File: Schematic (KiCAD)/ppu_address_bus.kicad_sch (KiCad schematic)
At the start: 59 parts, among them X3 INVERT

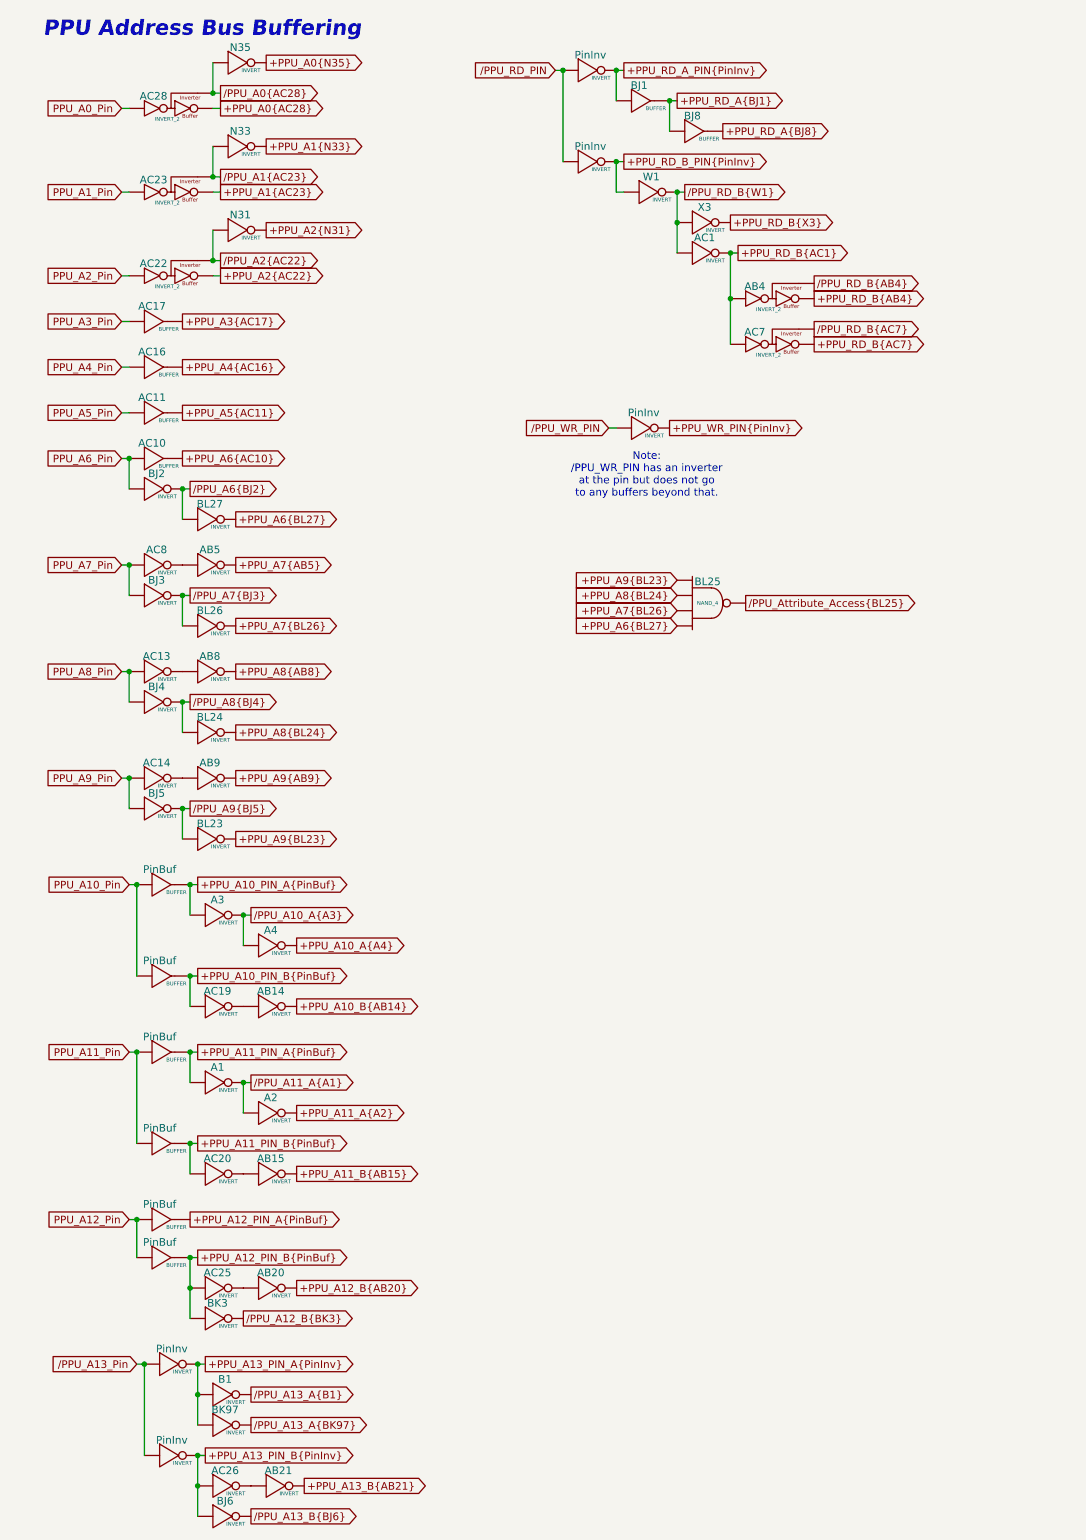
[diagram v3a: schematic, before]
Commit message: - All known gates and traces are now accounted for in the schematics!  :)
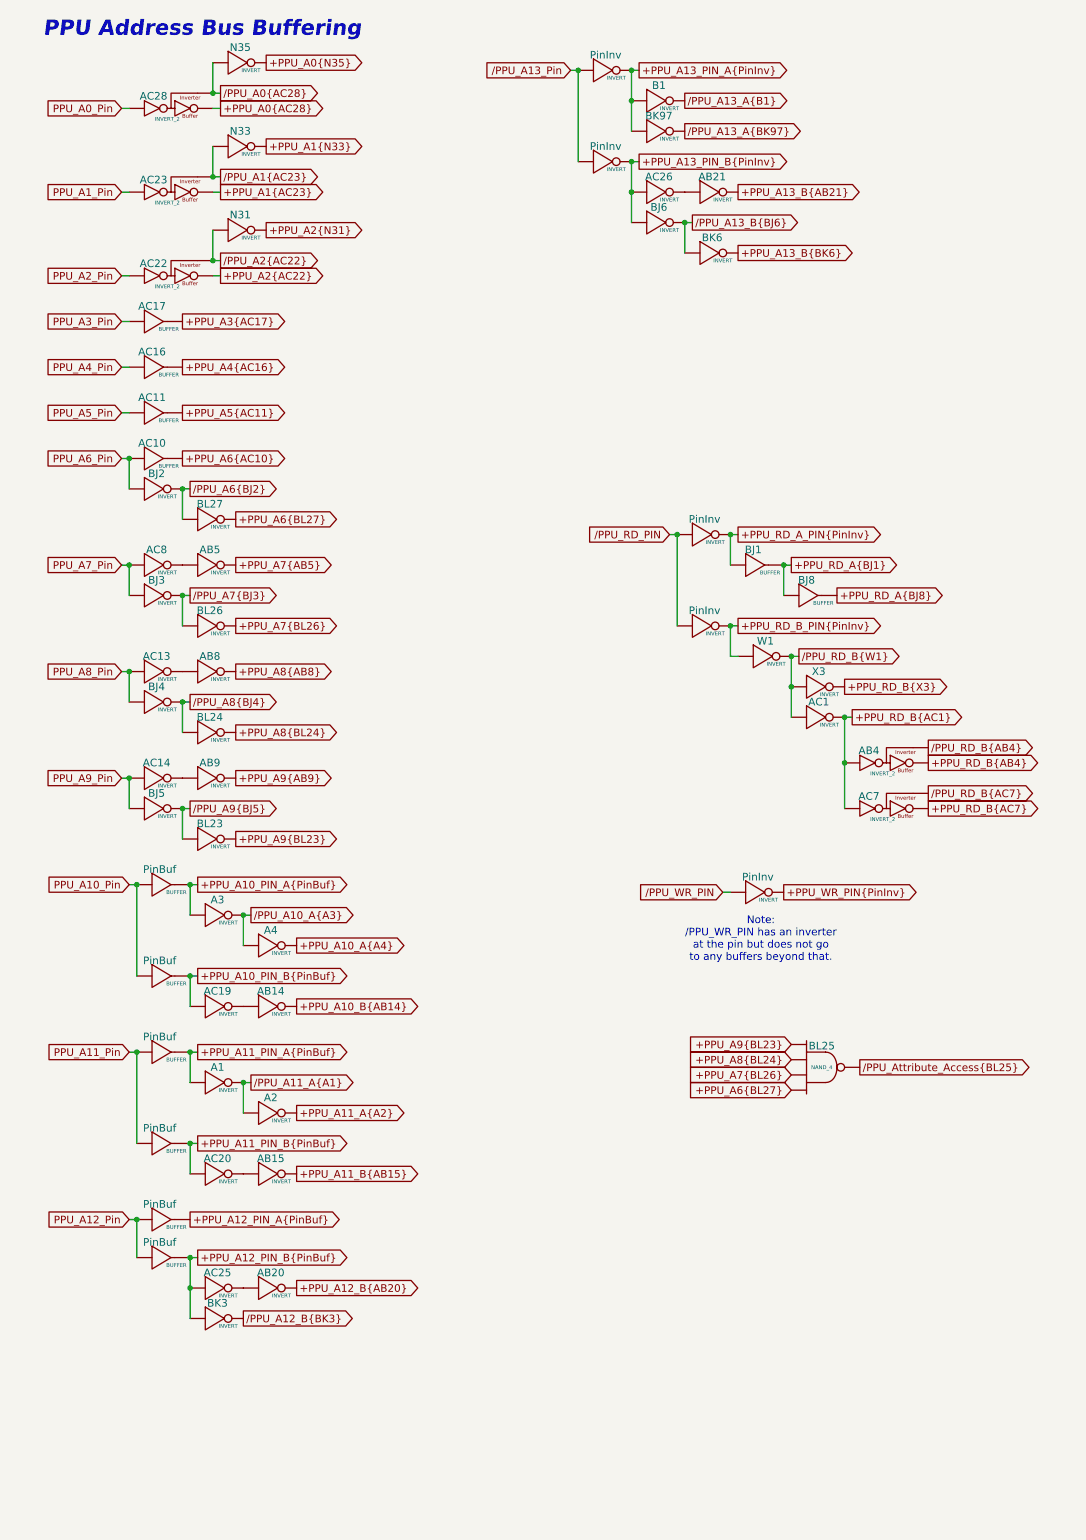
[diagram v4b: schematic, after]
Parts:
- added BK6: INVERT, symbol MMC5:INVERT
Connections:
- net /PPU_A13_B{BJ6}: now also BK6. (X)
- new net: AB21. (X), AC26. (X)
- new net: AB15. (X), AC20. (X)
- new net: AB5. (X), AC8. (X)
- new net: AB9. (X), AC14. (X)
- new net: AB20. (X), AC25. (X)
- new net: AB14. (X), AC19. (X)
- new net: AB8. (X), AC13. (X)
- new net +PPU_A13_B{BK6}: BK6. (X)
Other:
- moved on the sheet: AB21, AB4, AC1, AC26, AC7, B1, BJ1, BJ6, BJ8, BK97, BL25, PinInv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
